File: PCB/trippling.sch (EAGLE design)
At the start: 24 parts, among them K1 RELAY-SPDT-JZC-11F, K2 RELAY-SPDT-JZC-11F, T1 MMBT3904, T2 MMBT3904, X1 1751277

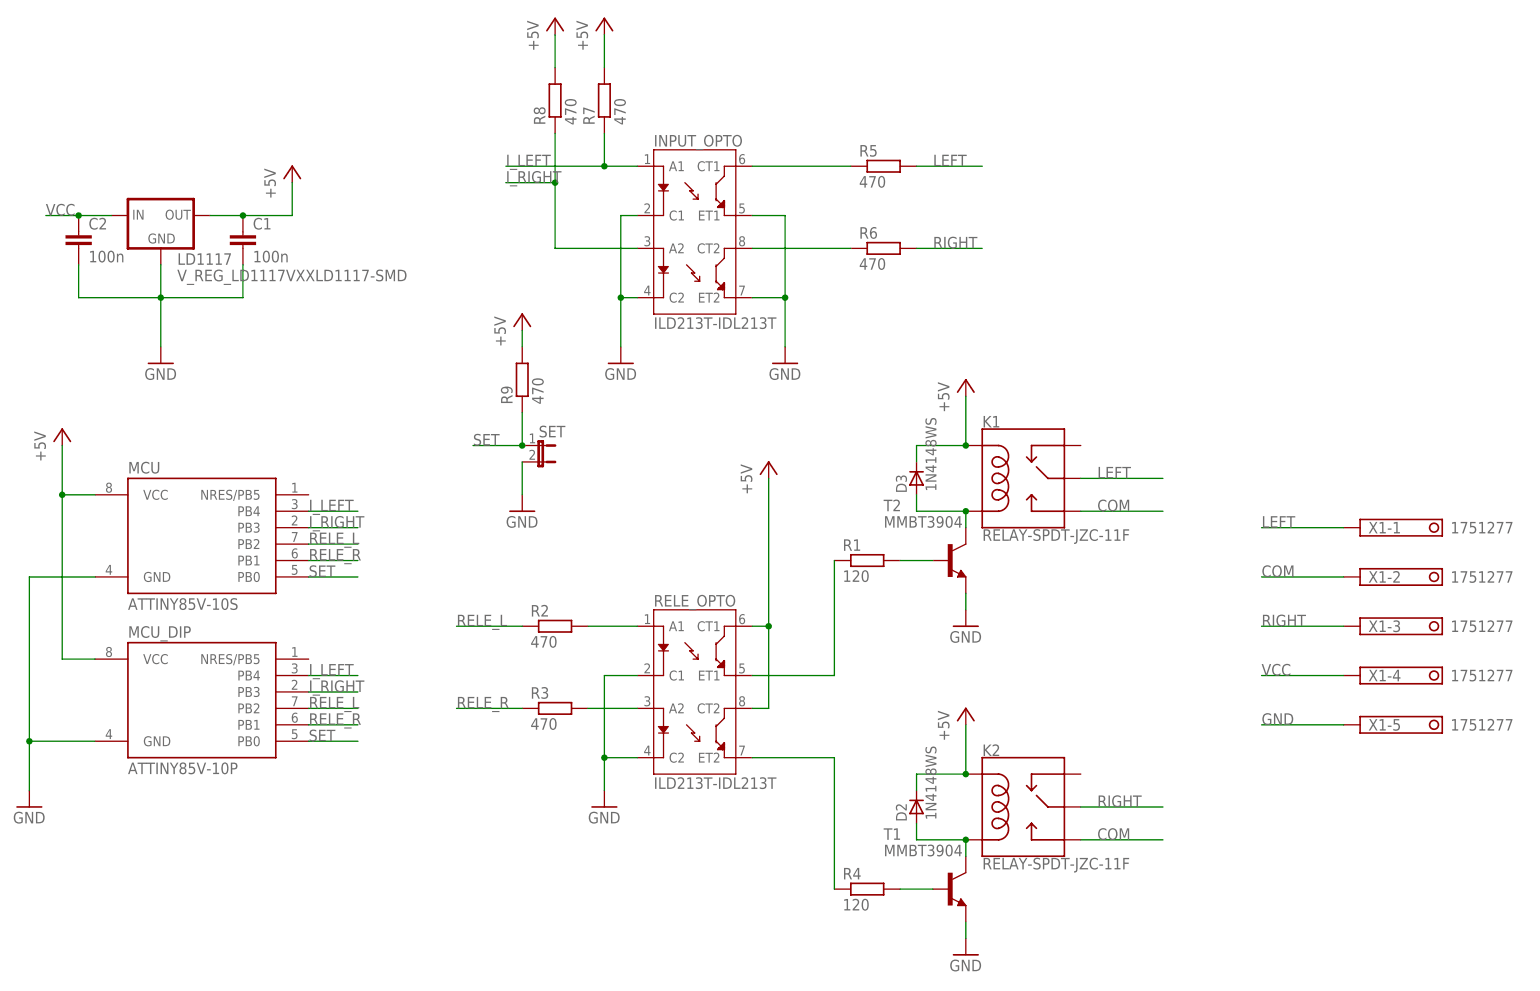
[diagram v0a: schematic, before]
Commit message: Fix HW pinout Fix SW pinout add documentation for AVR dragon
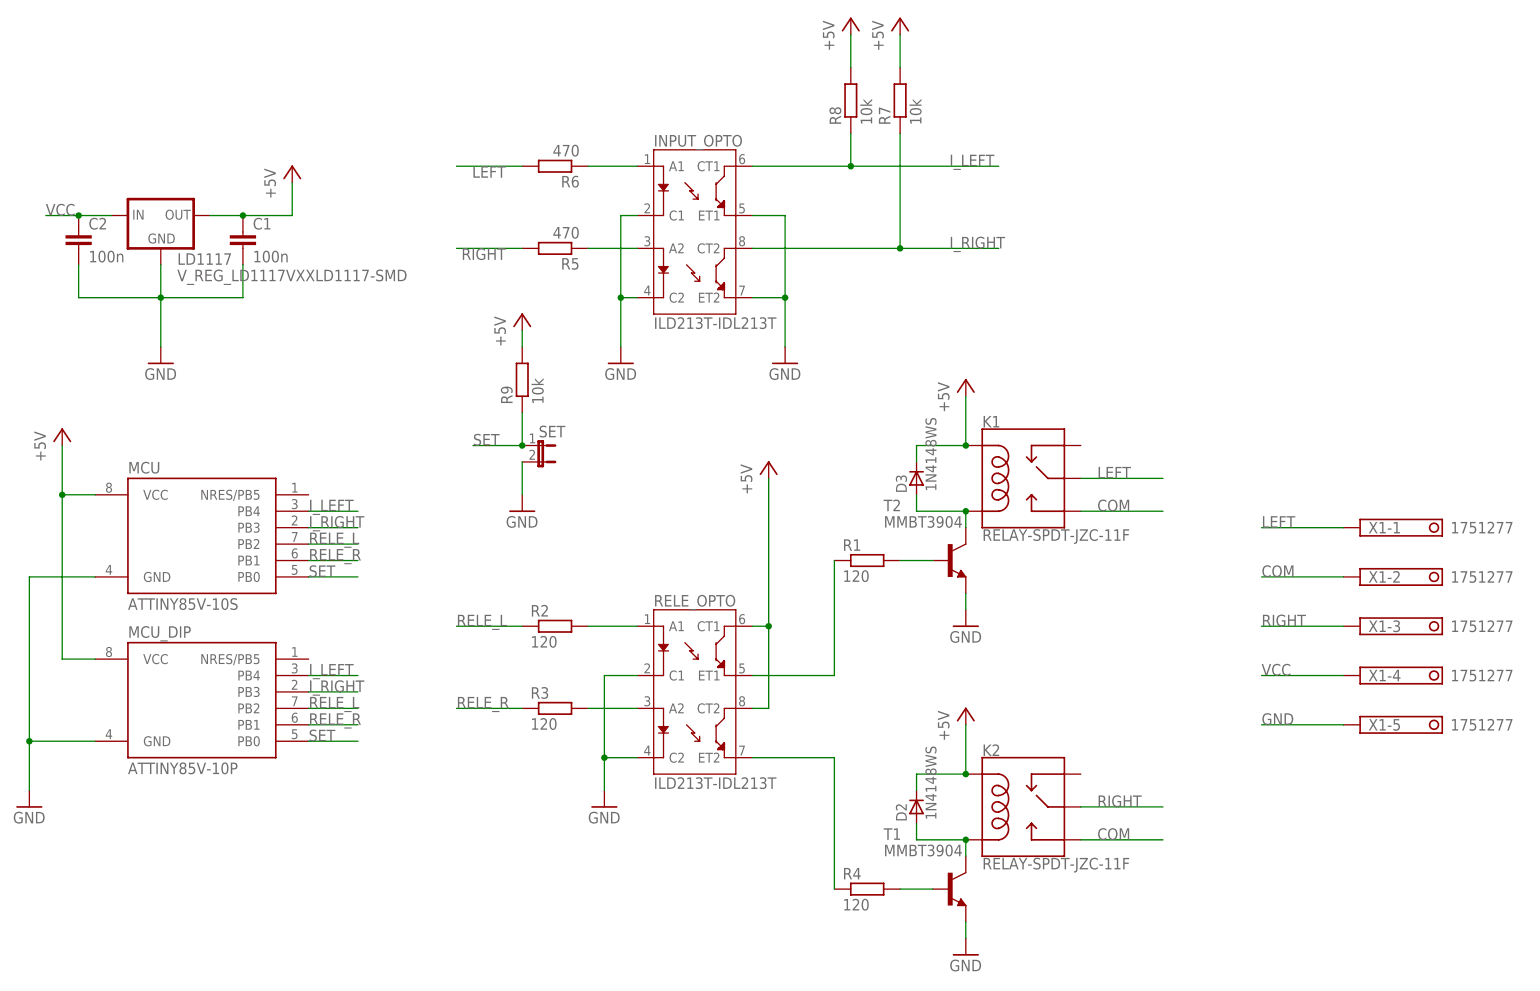
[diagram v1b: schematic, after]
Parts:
- R2, R3: value 470 -> 120
- R7, R8, R9: value 470 -> 10k
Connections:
- removed net N$5: INPUT_OPTO.CT1, R5.1
- removed net N$6: INPUT_OPTO.CT2, R6.1
- new net N$1: INPUT_OPTO.A1, R6.1
- new net N$2: INPUT_OPTO.A2, R5.1
- net I_LEFT: now also INPUT_OPTO.CT1, R8.1; no longer INPUT_OPTO.A1, R7.1
- net I_RIGHT: now also INPUT_OPTO.CT2, R7.1; no longer INPUT_OPTO.A2, R8.1
- net LEFT: now also R6.2; no longer R5.2
- net RIGHT: now also R5.2; no longer R6.2
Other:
- moved on the sheet: R5, R6, R7, R8
